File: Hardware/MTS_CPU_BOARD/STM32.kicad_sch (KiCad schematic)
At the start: 4 parts, among them U2 STM32G431K6Tx

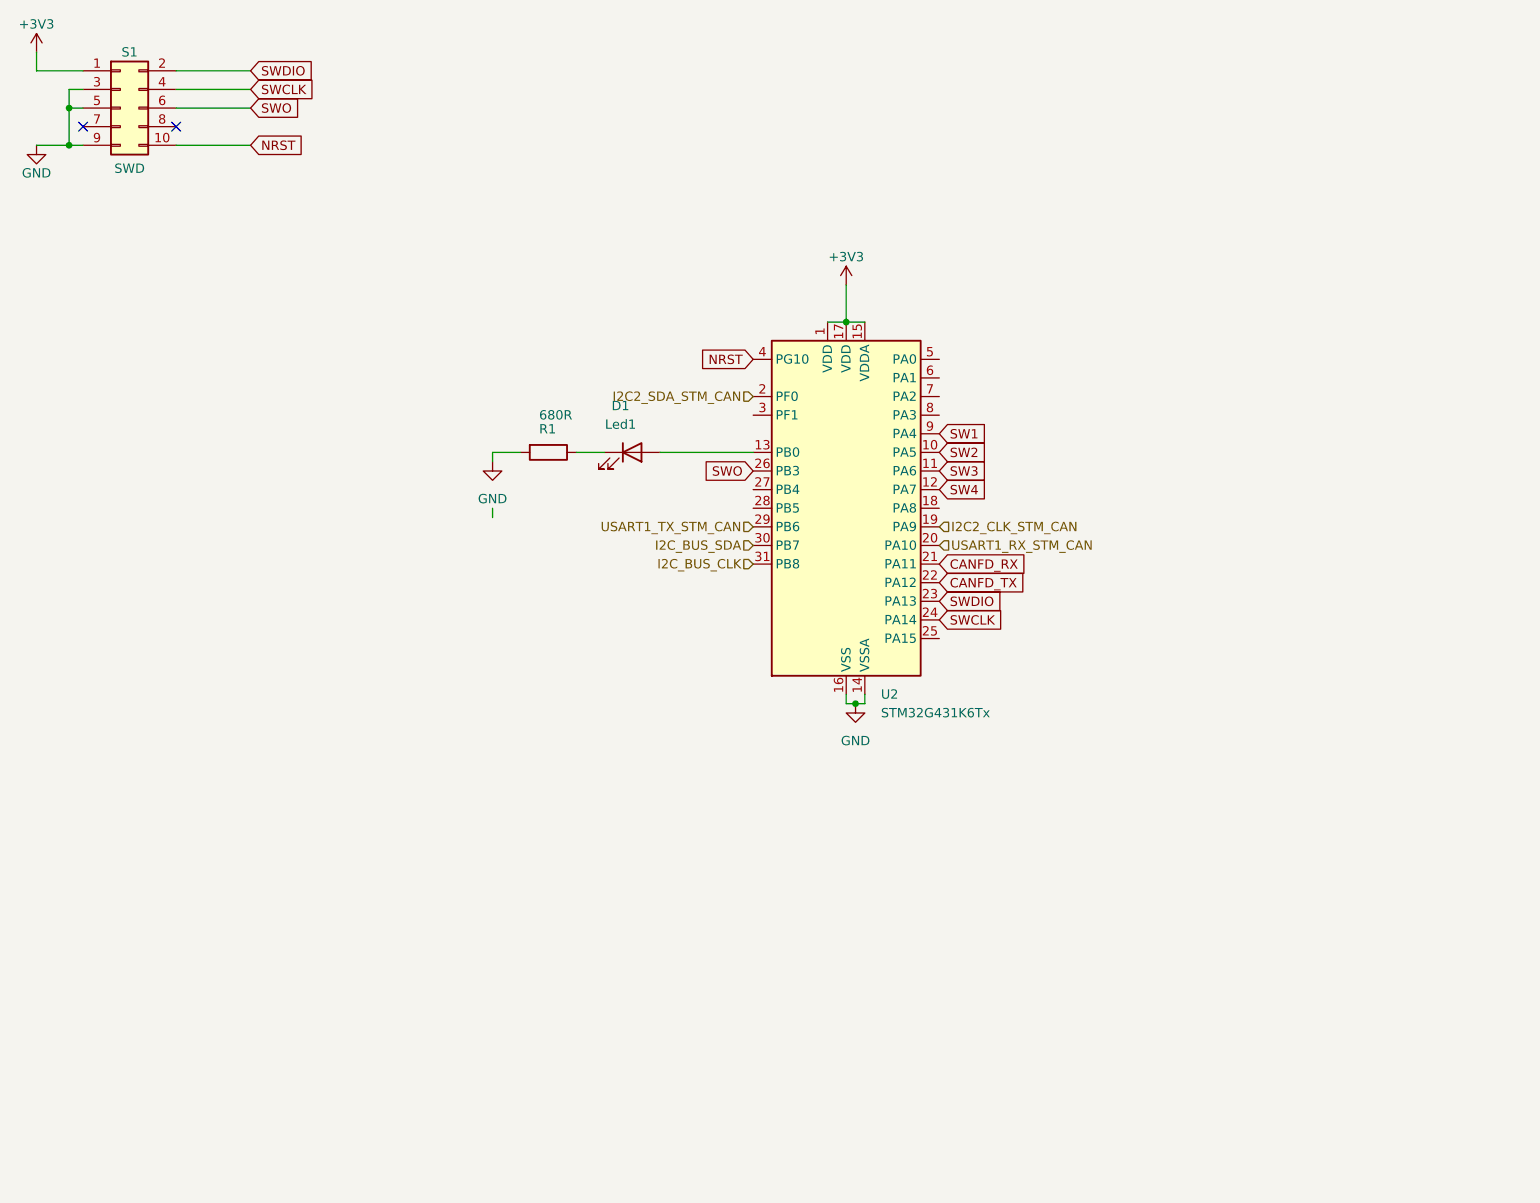
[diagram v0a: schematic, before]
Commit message: Add EtherCAT
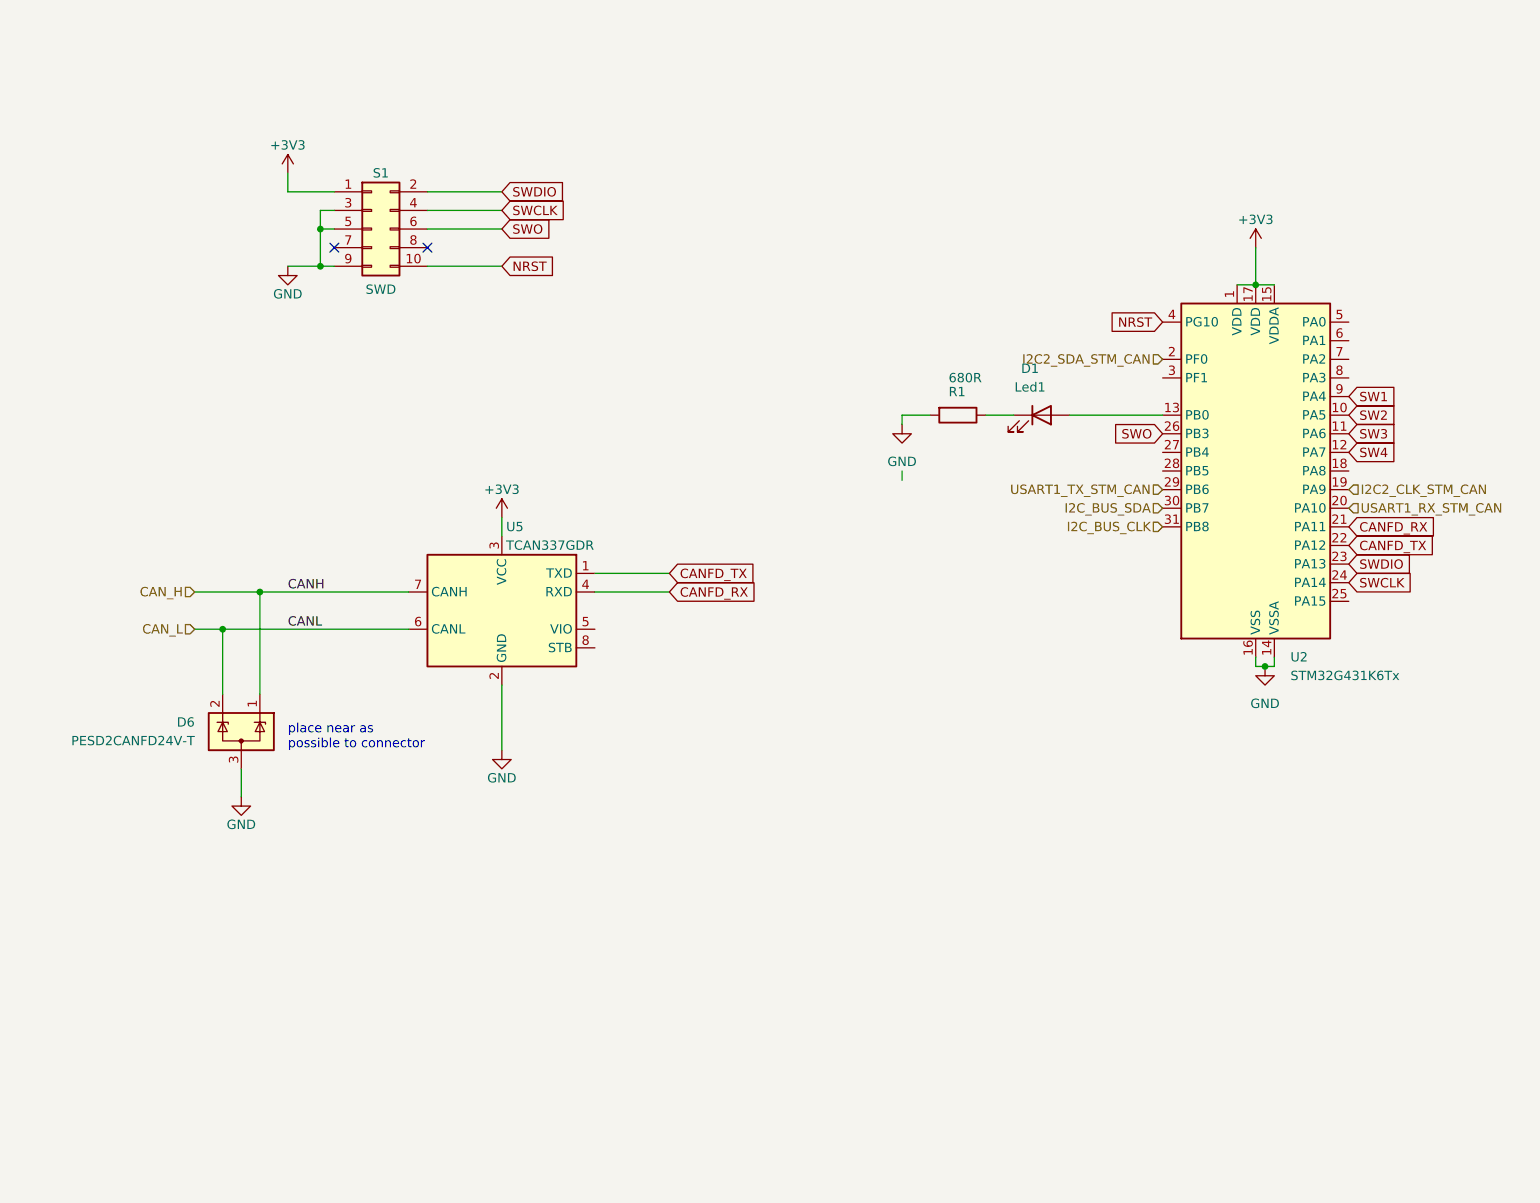
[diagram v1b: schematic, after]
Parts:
- added D6: PESD2CANFD24V-T, Package_TO_SOT_SMD:SOT-23, symbol Power_Protection:SP0502BAHT
- added U5: TCAN337GDR, Package_SO:SOIC-8_3.9x4.9mm_P1.27mm, symbol Interface_CAN_LIN:TJA1042T-3
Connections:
- net +3V3: now also U5.3 (VCC)
- net CANFD_RX: now also U5.4 (RXD)
- net CANFD_TX: now also U5.1 (TXD)
- net GND: now also D6.3 (A), U5.2 (GND)
- new net CAN_H: D6.1 (K), U5.7 (CANH)
- new net CAN_L: D6.2 (K), U5.6 (CANL)
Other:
- note added: "place near as possible to connector"
- moved on the sheet: D1, R1, S1, U2

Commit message: Add status Led´s
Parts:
- added U3: 24LC32, Package_SO:SOIC-8_3.9x4.9mm_P1.27mm, symbol Memory_EEPROM:24LC32
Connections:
- net +3V3: now also U3.8 (VCC)
- net GND: now also U3.1 (A0), U3.2 (A1), U3.3 (A2), U3.4 (GND)
- net I2C2_CLK_STM_CAN: now also U3.6 (SCL)
- net I2C2_SDA_STM_CAN: now also U3.5 (SDA)
- net USART1_RX_STM_CAN renamed USART1_RX_STM
- net USART1_TX_STM_CAN renamed USART1_TX_STM
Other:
- note added: "I2C Address 0xA0"
